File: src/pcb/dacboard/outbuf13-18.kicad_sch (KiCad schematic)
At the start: 18 parts, among them U71 AD8675ARZ, U72 AD8675ARZ, U73 AD8675ARZ, U74 AD8675ARZ, U75 AD8675ARZ, U76 AD8675ARZ

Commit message: dacboard routing
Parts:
- C59, C60, C61, C62, C63, C64: footprint (none) -> Capacitor_SMD:C_0603_1608Metric_Pad1.08x0.95mm_HandSolder
- R28, R29, R30, R31, R32, R33: footprint (none) -> Resistor_SMD:R_0805_2012Metric
- U71, U72, U73, U74, U75, U76: footprint R_8_ADI -> Package_SO:SOIC-8_3.9x4.9mm_P1.27mm
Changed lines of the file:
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@@
 			)
 		)
-		(property "Footprint" ""
+		(property "Footprint" "Resistor_SMD:R_0805_2012Metric"
 			(at 131.064 86.614 90)
 			(effects
@@
 			)
 		)
-		(property "Footprint" "R_8_ADI"
+		(property "Footprint" "Package_SO:SOIC-8_3.9x4.9mm_P1.27mm"
 			(at 186.69 82.55 0)
 			(effects
@@
 			)
 		)
-		(property "Footprint" "R_8_ADI"
+		(property "Footprint" "Package_SO:SOIC-8_3.9x4.9mm_P1.27mm"
 			(at 55.88 45.72 0)
 			(effects
@@
 			)
 		)
-		(property "Footprint" ""
+		(property "Footprint" "Resistor_SMD:R_0805_2012Metric"
 			(at 261.874 49.784 90)
 			(effects
@@
 			)
 		)
-		(property "Footprint" "R_8_ADI"
+		(property "Footprint" "Package_SO:SOIC-8_3.9x4.9mm_P1.27mm"
 			(at 186.69 45.72 0)
 			(effects
@@
 			)
 		)
-		(property "Footprint" ""
+		(property "Footprint" "Resistor_SMD:R_0805_2012Metric"
 			(at 131.064 128.524 90)
 			(effects
@@
 			)
 		)
-		(property "Footprint" ""
+		(property "Footprint" "Resistor_SMD:R_0805_2012Metric"
 			(at 131.064 49.784 90)
 			(effects
@@
 			)
 		)
-		(property "Footprint" ""
+		(property "Footprint" "Capacitor_SMD:C_0603_1608Metric_Pad1.08x0.95mm_HandSolder"
 			(at 169.8752 55.88 0)
 			(effects
@@
 			)
 		)
-		(property "Footprint" ""
+		(property "Footprint" "Capacitor_SMD:C_0603_1608Metric_Pad1.08x0.95mm_HandSolder"
 			(at 39.0652 134.62 0)
 			(effects
@@
 			)
 		)
-		(property "Footprint" ""
+		(property "Footprint" "Resistor_SMD:R_0805_2012Metric"
 			(at 261.874 86.614 90)
 			(effects
@@
 			)
 		)
-		(property "Footprint" ""
+		(property "Footprint" "Capacitor_SMD:C_0603_1608Metric_Pad1.08x0.95mm_HandSolder"
 			(at 39.0652 92.71 0)
 			(effects
@@
 			)
 		)
-		(property "Footprint" "R_8_ADI"
+		(property "Footprint" "Package_SO:SOIC-8_3.9x4.9mm_P1.27mm"
 			(at 55.88 124.46 0)
 			(effects
@@
 			)
 		)
-		(property "Footprint" ""
+		(property "Footprint" "Capacitor_SMD:C_0603_1608Metric_Pad1.08x0.95mm_HandSolder"
 			(at 169.8752 132.08 0)
 			(effects
@@
 			)
 		)
-		(property "Footprint" "R_8_ADI"
+		(property "Footprint" "Package_SO:SOIC-8_3.9x4.9mm_P1.27mm"
 			(at 186.69 121.92 0)
 			(effects
@@
 			)
 		)
-		(property "Footprint" ""
+		(property "Footprint" "Resistor_SMD:R_0805_2012Metric"
 			(at 261.874 125.984 90)
 			(effects
@@
 			)
 		)
-		(property "Footprint" ""
+		(property "Footprint" "Capacitor_SMD:C_0603_1608Metric_Pad1.08x0.95mm_HandSolder"
 			(at 169.8752 92.71 0)
 			(effects
@@
 			)
 		)
-		(property "Footprint" ""
+		(property "Footprint" "Capacitor_SMD:C_0603_1608Metric_Pad1.08x0.95mm_HandSolder"
 			(at 39.0652 55.88 0)
 			(effects
@@
 			)
 		)
-		(property "Footprint" "R_8_ADI"
+		(property "Footprint" "Package_SO:SOIC-8_3.9x4.9mm_P1.27mm"
 			(at 55.88 82.55 0)
 			(effects

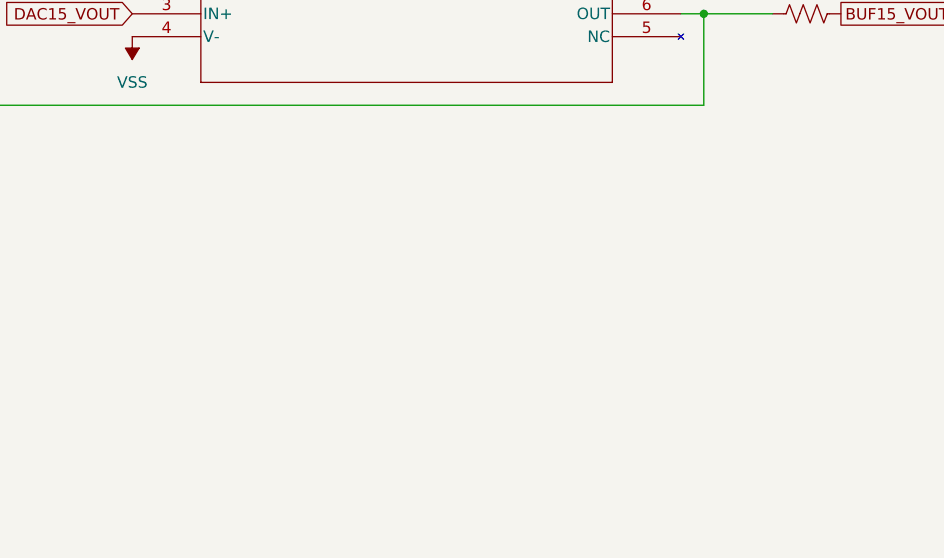
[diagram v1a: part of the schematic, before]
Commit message: got rid of all drc errors
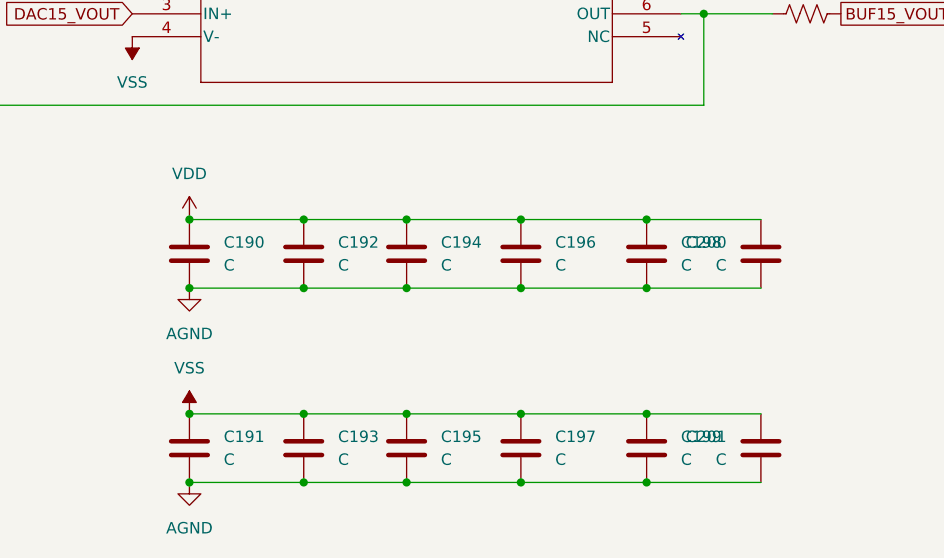
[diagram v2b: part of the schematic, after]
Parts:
- added C190, C191, C192, C193, C194, C195, C196, C197, C198, C199, C200, C201: C, Capacitor_SMD:C_0402_1005Metric_Pad0.74x0.62mm_HandSolder, symbol Device:C
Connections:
- net VDD: now also C190.1, C192.1, C194.1, C196.1, C198.1, C200.1
- net VSS: now also C191.1, C193.1, C195.1, C197.1, C199.1, C201.1
- new net AGND: C190.2, C191.2, C192.2, C193.2, C194.2, C195.2, C196.2, C197.2, C198.2, C199.2, C200.2, C201.2
